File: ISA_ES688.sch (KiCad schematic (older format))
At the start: 112 parts, among them J1 LINE IN, J11 ISA BUS, J2 LINE OUT, J3 Joystick/MIDI, J7 SPKR OUT, J8 MIC, U1 L78L05, U2 74LS14, U7 LM1877, Y1 14.318Mhz

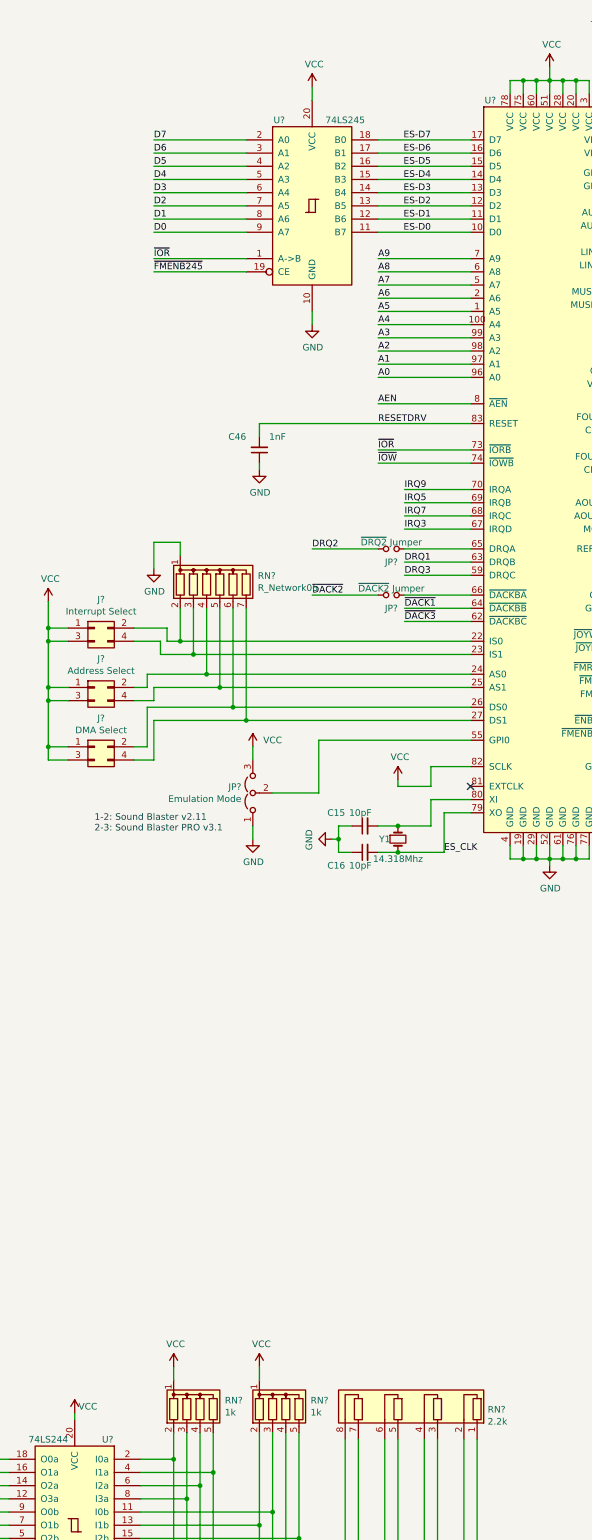
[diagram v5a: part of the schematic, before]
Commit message: Begin assigning footprints
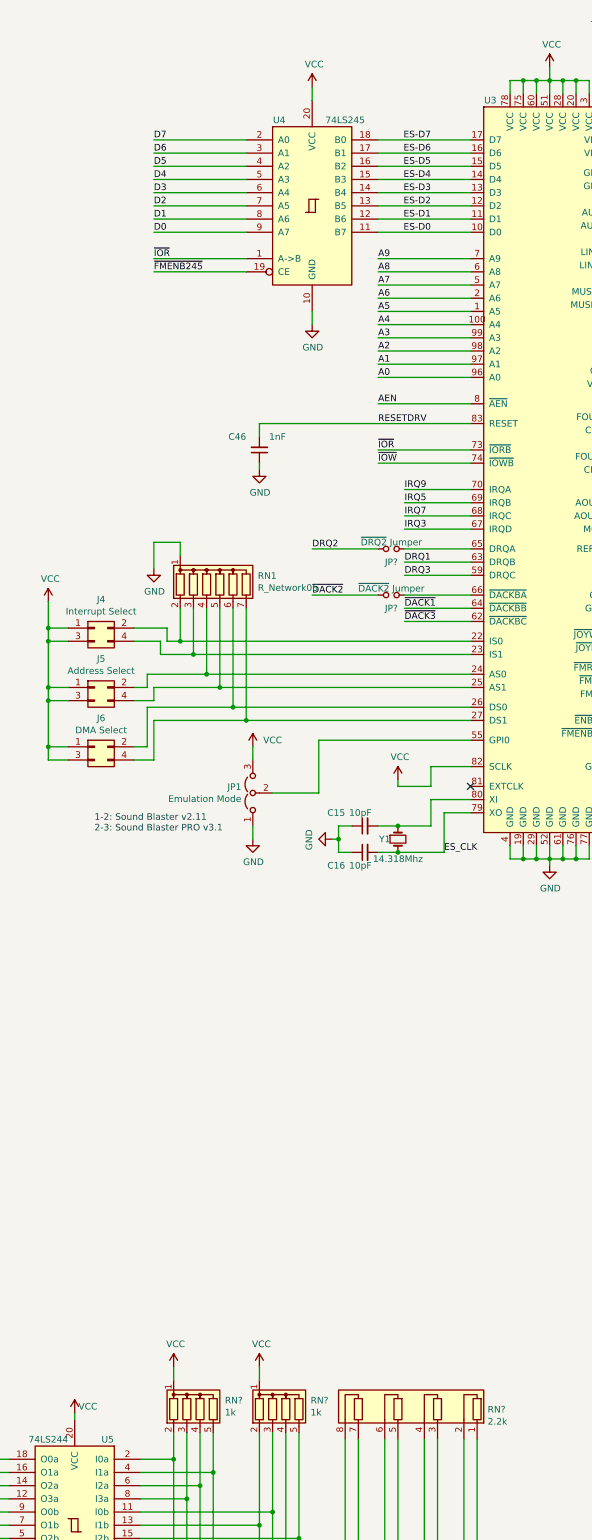
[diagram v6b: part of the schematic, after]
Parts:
- J4, J5, J6: renamed from J?; footprint (none) -> Connector_PinHeader_2.54mm:PinHeader_2x02_P2.54mm_Vertical
- JP1: renamed from JP?; footprint (none) -> Connector_PinHeader_2.54mm:PinHeader_1x03_P2.54mm_Vertical
- RV1: footprint (none) -> Volume_Pot:PTD902
- U4, U5: renamed from U?; footprint (none) -> Package_SO:SOIC-20W_7.5x12.8mm_P1.27mm
- gave numbers to parts that had none: 2
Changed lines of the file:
@@
 NoConn ~ 2300 8550
 $Comp
-L 74xx:74LS245 U?
+L 74xx:74LS245 U4
 U 1 1 60CF4739
 P 10200 2300
-F 0 "U?" H 9950 2950 50  0000 C CNN
+F 0 "U4" H 9950 2950 50  0000 C CNN
 F 1 "74LS245" H 10450 2950 50  0000 C CNN
-F 2 "" H 10200 2300 50  0001 C CNN
+F 2 "Package_SO:SOIC-20W_7.5x12.8mm_P1.27mm" H 10200 2300 50  0001 C CNN
 F 3 "http://www.ti.com/lit/gpn/sn74LS245" H 10200 2300 50  0001 C CNN
 	1    10200 2300
@@
 $EndComp
 $Comp
-L 74xx:74LS244 U?
+L 74xx:74LS244 U5
 U 1 1 60CF5E2D
 P 8400 12300
-F 0 "U?" H 8150 12950 50  0000 C CNN
+F 0 "U5" H 8150 12950 50  0000 C CNN
 F 1 "74LS244" H 8600 12950 50  0000 C CNN
-F 2 "" H 8400 12300 50  0001 C CNN
+F 2 "Package_SO:SOIC-20W_7.5x12.8mm_P1.27mm" H 8400 12300 50  0001 C CNN
 F 3 "http://www.ti.com/lit/ds/symlink/sn74ls244.pdf" H 8400 12300 50  0001 C CNN
 	1    8400 12300
@@
 $EndComp
 $Comp
-L custom_components:ES688F U?
+L custom_components:ES688F U3
 U 1 1 60CF110B
 P 12000 4400
-F 0 "U?" H 11550 7300 50  0000 C CNN
+F 0 "U3" H 11550 7300 50  0000 C CNN
 F 1 "ES688F" H 12500 7300 50  0000 C CNN
 F 2 "Package_QFP:LQFP-14x20mm_P0.5mm" H 12000 5350 50  0001 C CNN
@@
 	11400 5350 10900 5350
 $Comp
-L Connector_Generic:Conn_02x02_Odd_Even J?
+L Connector_Generic:Conn_02x02_Odd_Even J4
 U 1 1 62AED216
 P 8550 5500
-F 0 "J?" H 8600 5717 50  0000 C CNN
+F 0 "J4" H 8600 5717 50  0000 C CNN
 F 1 "Interrupt Select" H 8600 5626 50  0000 C CNN
-F 2 "" H 8550 5500 50  0001 C CNN
+F 2 "Connector_PinHeader_2.54mm:PinHeader_2x02_P2.54mm_Vertical" H 8550 5500 50  0001 C CNN
 F 3 "~" H 8550 5500 50  0001 C CNN
 	1    8550 5500
@@
 	9000 4850 9000 5050
 $Comp
-L Connector_Generic:Conn_02x02_Odd_Even J?
+L Connector_Generic:Conn_02x02_Odd_Even J5
 U 1 1 62BE0014
 P 8550 5950
-F 0 "J?" H 8600 6167 50  0000 C CNN
+F 0 "J5" H 8600 6167 50  0000 C CNN
 F 1 "Address Select" H 8600 6076 50  0000 C CNN
-F 2 "" H 8550 5950 50  0001 C CNN
+F 2 "Connector_PinHeader_2.54mm:PinHeader_2x02_P2.54mm_Vertical" H 8550 5950 50  0001 C CNN
 F 3 "~" H 8550 5950 50  0001 C CNN
 	1    8550 5950
@@
 $EndComp
 $Comp
-L Connector_Generic:Conn_02x02_Odd_Even J?
+L Connector_Generic:Conn_02x02_Odd_Even J6
 U 1 1 62BE0F99
 P 8550 6400
-F 0 "J?" H 8600 6617 50  0000 C CNN
+F 0 "J6" H 8600 6617 50  0000 C CNN
 F 1 "DMA Select" H 8600 6526 50  0000 C CNN
-F 2 "" H 8550 6400 50  0001 C CNN
+F 2 "Connector_PinHeader_2.54mm:PinHeader_2x02_P2.54mm_Vertical" H 8550 6400 50  0001 C CNN
 F 3 "~" H 8550 6400 50  0001 C CNN
 	1    8550 6400
@@
 Connection ~ 13850 1000
 $Comp
-L Device:R_Network06 RN?
+L Device:R_Network06 RN1
 U 1 1 674F16B7
 P 9500 5150
-F 0 "RN?" H 9788 5196 50  0000 L CNN
+F 0 "RN1" H 9788 5196 50  0000 L CNN
 F 1 "R_Network06" H 9788 5105 50  0000 L CNN
 F 2 "Resistor_THT:R_Array_SIP7" V 9875 5150 50  0001 C CNN
@@
 Connection ~ 20900 10250
 $Comp
-L Jumper:Jumper_3_Open JP?
+L Jumper:Jumper_3_Open JP1
 U 1 1 62275D16
 P 9750 6750
-F 0 "JP?" V 9796 6837 50  0000 L CNN
+F 0 "JP1" V 9796 6837 50  0000 L CNN
 F 1 "Emulation Mode" V 9705 6837 50  0000 L CNN
-F 2 "" H 9750 6750 50  0001 C CNN
+F 2 "Connector_PinHeader_2.54mm:PinHeader_1x03_P2.54mm_Vertical" H 9750 6750 50  0001 C CNN
 F 3 "~" H 9750 6750 50  0001 C CNN
 	1    9750 6750
@@
 F 0 "RV1" V 17950 4450 50  0000 R CNN
 F 1 "Volume Knob" V 17850 4750 50  0000 R CNN
-F 2 "" H 17650 4175 50  0001 C CNN
+F 2 "Volume_Pot:PTD902" H 17650 4175 50  0001 C CNN
 F 3 "~" H 17650 4175 50  0001 C CNN
 	1    17400 4250

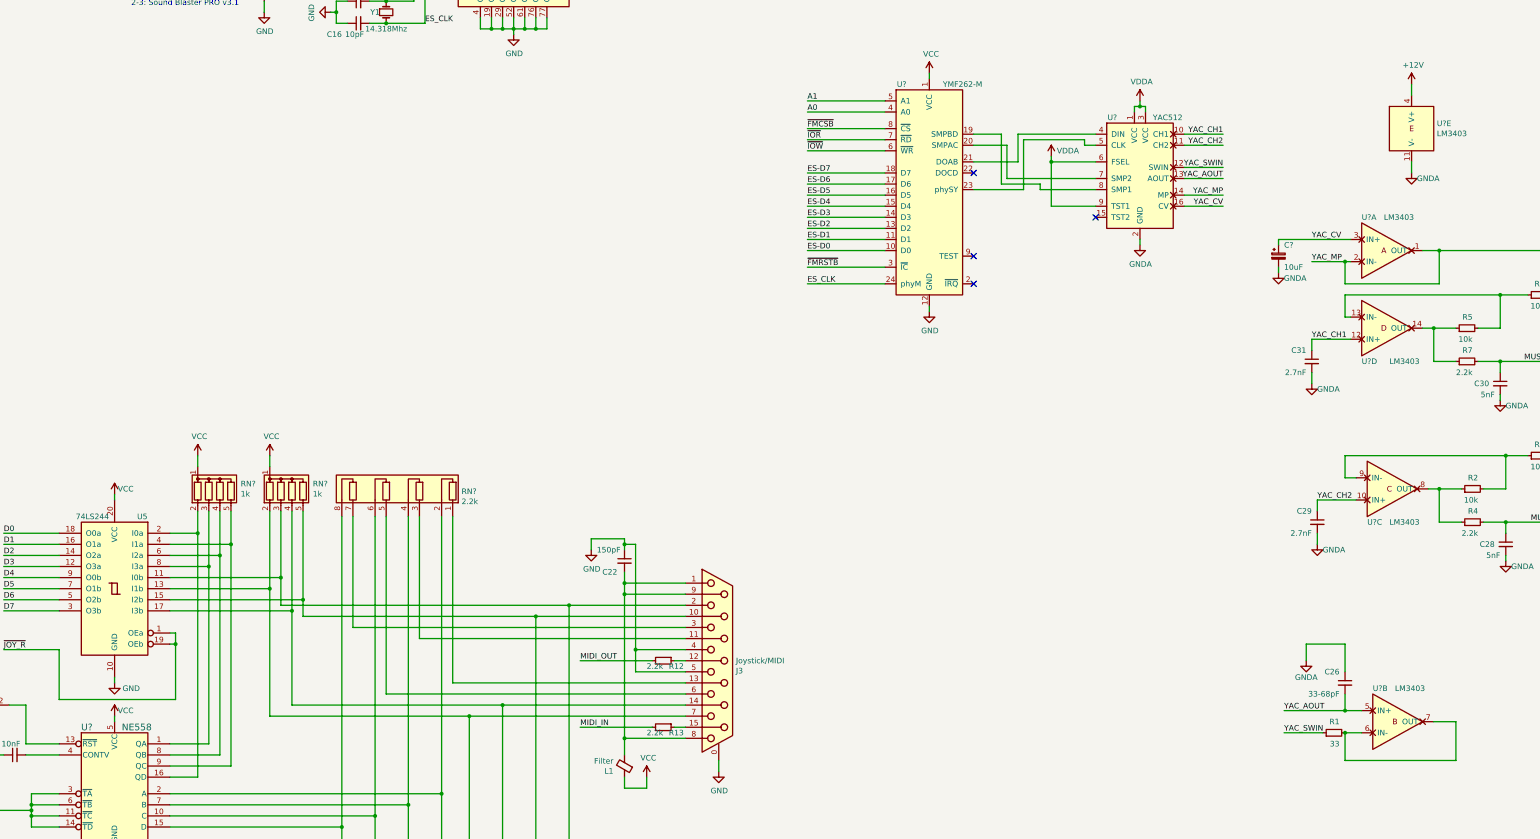
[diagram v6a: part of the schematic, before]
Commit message: Assign more footprints
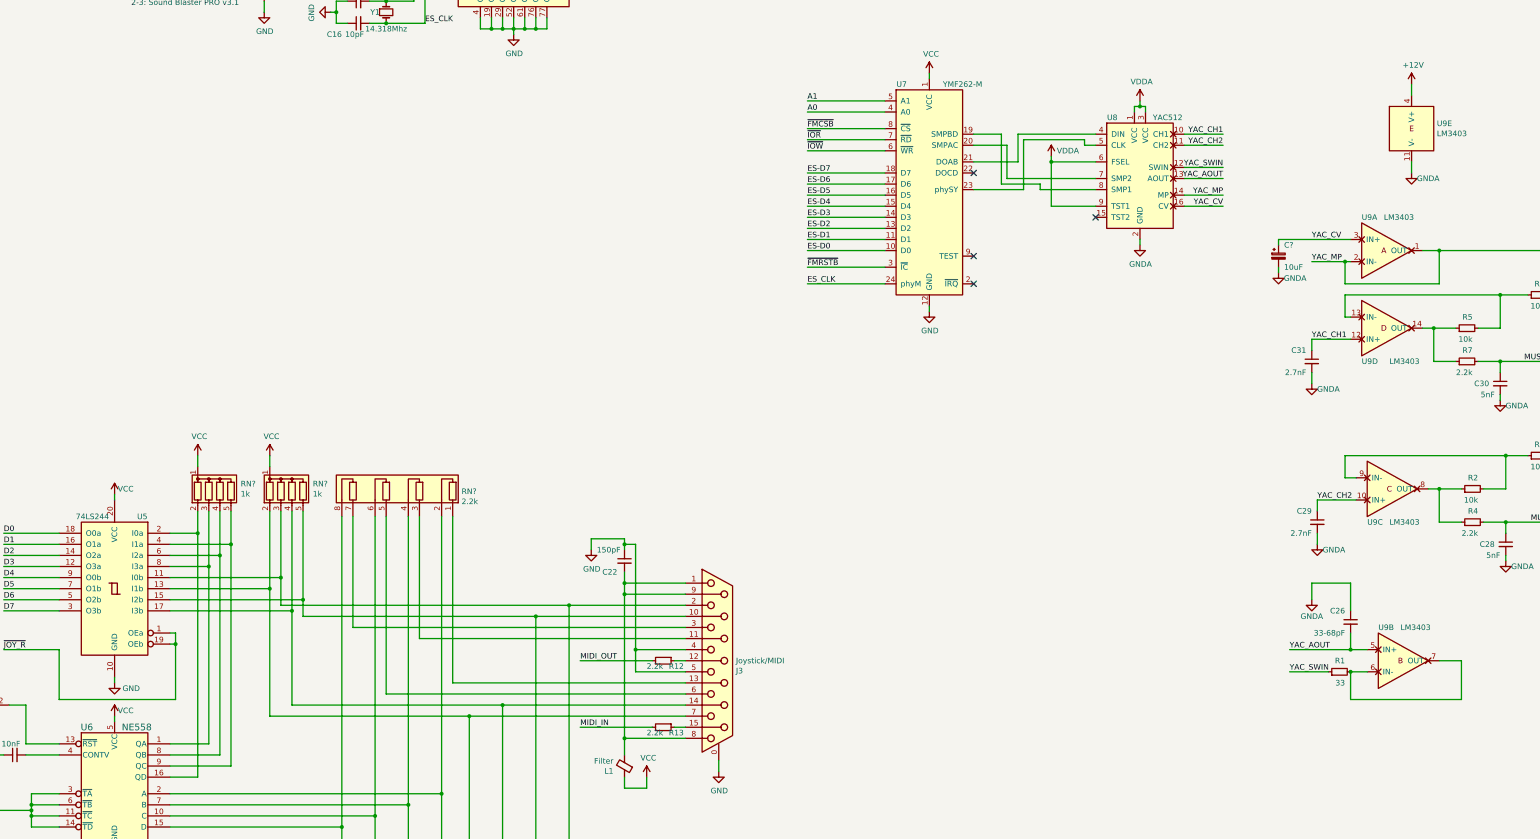
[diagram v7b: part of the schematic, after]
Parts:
- U7: renamed from U?; footprint (none) -> Package_SO:SOIC-24W_7.5x15.4mm_P1.27mm
- U8: renamed from U?; footprint (none) -> Package_SO:SO-16_3.9x9.9mm_P1.27mm
- U9: renamed from U?; footprint (none) -> Package_DIP:DIP-14_W7.62mm
- gave numbers to parts that had none: 1
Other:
- moved on the sheet: C26, R1, U9B
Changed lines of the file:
@@
 $EndComp
 $Comp
-L custom_components:NE558 U?
+L custom_components:NE558 U6
 U 1 1 60D93AFC
 P 8400 14300
-F 0 "U?" H 8150 15050 60  0000 C CNN
+F 0 "U6" H 8150 15050 60  0000 C CNN
 F 1 "NE558" H 8600 15050 60  0000 C CNN
 F 2 "" H 8900 14500 60  0000 C CNN
@@
 $EndComp
 $Comp
-L custom_components:YMF262-M U?
+L custom_components:YMF262-M U7
 U 1 1 675C24EF
 P 15750 8650
-F 0 "U?" H 15500 9550 50  0000 C CNN
+F 0 "U7" H 15500 9550 50  0000 C CNN
 F 1 "YMF262-M" H 16050 9550 50  0000 C CNN
-F 2 "" H 15750 8650 50  0001 C CNN
+F 2 "Package_SO:SOIC-24W_7.5x15.4mm_P1.27mm" H 15750 8650 50  0001 C CNN
 F 3 "" H 15750 8650 50  0001 C CNN
 	1    15750 8650
@@
 $EndComp
 $Comp
-L custom_components:YAC512 U?
+L custom_components:YAC512 U8
 U 1 1 675C3A96
 P 17650 8550
-F 0 "U?" H 17400 9050 50  0000 C CNN
+F 0 "U8" H 17400 9050 50  0000 C CNN
 F 1 "YAC512" H 17900 9050 50  0000 C CNN
-F 2 "" H 17650 7950 50  0001 C CNN
+F 2 "Package_SO:SO-16_3.9x9.9mm_P1.27mm" H 17650 7950 50  0001 C CNN
 F 3 "" H 17650 7950 50  0001 C CNN
 	1    17650 8550
@@
 $EndComp
 $Comp
-L custom_components:LM3403 U?
+L custom_components:LM3403 U9
 U 5 1 675C4E4C
 P 20100 8150
-F 0 "U?" H 20328 8196 50  0000 L CNN
+F 0 "U9" H 20328 8196 50  0000 L CNN
 F 1 "LM3403" H 20328 8105 50  0000 L CNN
-F 2 "" H 20100 8150 50  0001 C CNN
+F 2 "Package_DIP:DIP-14_W7.62mm" H 20100 8150 50  0001 C CNN
 F 3 "" H 20100 8150 50  0001 C CNN
 	5    20100 8150
@@
 NoConn ~ 16150 8550
 $Comp
-L custom_components:LM3403 U?
+L custom_components:LM3403 U9
 U 1 1 618A860C
 P 19850 9250
-F 0 "U?" H 19650 9550 50  0000 L CNN
+F 0 "U9" H 19650 9550 50  0000 L CNN
 F 1 "LM3403" H 19850 9550 50  0000 L CNN
-F 2 "" H 19850 9250 50  0001 C CNN
+F 2 "Package_DIP:DIP-14_W7.62mm" H 19850 9250 50  0001 C CNN
 F 3 "" H 19850 9250 50  0001 C CNN
 	1    19850 9250
@@
 $EndComp
 $Comp
-L custom_components:LM3403 U?
+L custom_components:LM3403 U9
 U 2 1 618ABB59
-P 19950 13500
-F 0 "U?" H 19750 13800 50  0000 L CNN
-F 1 "LM3403" H 19950 13800 50  0000 L CNN
-F 2 "" H 19950 13500 50  0001 C CNN
-F 3 "" H 19950 13500 50  0001 C CNN
-	2    19950 13500
-	1    0    0    -1
-$EndComp
-$Comp
-L custom_components:LM3403 U?
+P 20000 12950
+F 0 "U9" H 19800 13250 50  0000 L CNN
+F 1 "LM3403" H 20000 13250 50  0000 L CNN
+F 2 "Package_DIP:DIP-14_W7.62mm" H 20000 12950 50  0001 C CNN
+F 3 "" H 20000 12950 50  0001 C CNN
+	2    20000 12950
+	1    0    0    -1
+$EndComp
+$Comp
+L custom_components:LM3403 U9
 U 3 1 6191F91E
 P 19900 11400
-F 0 "U?" H 19700 11700 50  0000 L CNN
+F 0 "U9" H 19700 11700 50  0000 L CNN
 F 1 "LM3403" H 19900 11700 50  0000 L CNN
-F 2 "" H 19900 11400 50  0001 C CNN
+F 2 "Package_DIP:DIP-14_W7.62mm" H 19900 11400 50  0001 C CNN
 F 3 "" H 19900 11400 50  0001 C CNN
 	3    19900 11400
@@
 YAC_CH1
 $Comp
-L custom_components:LM3403 U?
+L custom_components:LM3403 U9
 U 4 1 61994965
 P 19850 9950
-F 0 "U?" H 19650 10250 50  0000 L CNN
+F 0 "U9" H 19650 10250 50  0000 L CNN
 F 1 "LM3403" H 19900 10250 50  0000 L CNN
-F 2 "" H 19850 9950 50  0001 C CNN
+F 2 "Package_DIP:DIP-14_W7.62mm" H 19850 9950 50  0001 C CNN
 F 3 "" H 19850 9950 50  0001 C CNN
 	4    19850 9950
@@
 Text Label 18400 8600 2    50   ~ 0
 YAC_AOUT
-Text Label 18950 13400 0    50   ~ 0
+Text Label 19000 12850 0    50   ~ 0
 YAC_AOUT
 Wire Wire Line
-	18950 13400 19500 13400
+	19000 12850 19550 12850
 $Comp
 L Device:C_Small C26
 U 1 1 62A2E09E
-P 19500 13150
-F 0 "C26" H 19550 13250 50  0000 L CNN
-F 1 "33-68pF" H 19550 13050 50  0000 L CNN
-F 2 "Capacitor_THT:C_Disc_D6.0mm_W2.5mm_P5.00mm" H 19500 13150 50  0001 C CNN
-F 3 "~" H 19500 13150 50  0001 C CNN
-	1    19500 13150
+P 19550 12600
+F 0 "C26" H 19600 12700 50  0000 L CNN
+F 1 "33-68pF" H 19600 12500 50  0000 L CNN
+F 2 "Capacitor_THT:C_Disc_D6.0mm_W2.5mm_P5.00mm" H 19550 12600 50  0001 C CNN
+F 3 "~" H 19550 12600 50  0001 C CNN
+	1    19550 12600
 	-1   0    0    -1
 $EndComp
 Wire Wire Line
-	19500 13250 19500 13400
-Connection ~ 19500 13400
-Wire Wire Line
-	19500 13400 19650 13400
+	19550 12700 19550 12850
+Connection ~ 19550 12850
+Wire Wire Line
+	19550 12850 19700 12850
 $Comp
 L power:GNDA #PWR?
 U 1 1 62AAAABD
-P 19150 12950
-F 0 "#PWR?" H 19150 12700 50  0001 C CNN
-F 1 "GNDA" H 19150 12800 50  0000 C CNN
-F 2 "" H 19150 12950 50  0001 C CNN
-F 3 "" H 19150 12950 50  0001 C CNN
-	1    19150 12950
-	1    0    0    -1
-$EndComp
-Wire Wire Line
-	19500 13050 19500 12800
-Wire Wire Line
-	19500 12800 19150 12800
-Wire Wire Line
-	19150 12800 19150 12950
-Wire Wire Line
-	20300 13500 20500 13500
-Wire Wire Line
-	20500 13500 20500 13850
-Wire Wire Line
-	20500 13850 19500 13850
-Wire Wire Line
-	19500 13850 19500 13600
-Wire Wire Line
-	19500 13600 19650 13600
+P 19200 12400
+F 0 "#PWR?" H 19200 12150 50  0001 C CNN
+F 1 "GNDA" H 19200 12250 50  0000 C CNN
+F 2 "" H 19200 12400 50  0001 C CNN
+F 3 "" H 19200 12400 50  0001 C CNN
+	1    19200 12400
+	1    0    0    -1
+$EndComp
+Wire Wire Line
+	19550 12500 19550 12250
+Wire Wire Line
+	19550 12250 19200 12250
+Wire Wire Line
+	19200 12250 19200 12400
+Wire Wire Line
+	20350 12950 20550 12950
+Wire Wire Line
+	20550 12950 20550 13300
+Wire Wire Line
+	20550 13300 19550 13300
+Wire Wire Line
+	19550 13300 19550 13050
+Wire Wire Line
+	19550 13050 19700 13050
 $Comp
 L Device:R_Small R1
 U 1 1 62CA2E14
-P 19400 13600
-F 0 "R1" V 19500 13550 50  0000 L CNN
-F 1 "33" V 19300 13550 50  0000 L CNN
-F 2 "Resistor_THT:R_Axial_DIN0207_L6.3mm_D2.5mm_P7.62mm_Horizontal" H 19400 13600 50  0001 C CNN
-F 3 "~" H 19400 13600 50  0001 C CNN
-	1    19400 13600
+P 19450 13050
+F 0 "R1" V 19550 13000 50  0000 L CNN
+F 1 "33" V 19350 13000 50  0000 L CNN
+F 2 "Resistor_THT:R_Axial_DIN0207_L6.3mm_D2.5mm_P7.62mm_Horizontal" H 19450 13050 50  0001 C CNN
+F 3 "~" H 19450 13050 50  0001 C CNN
+	1    19450 13050
 	0    -1   -1   0
 $EndComp
-Connection ~ 19500 13600
-Wire Wire Line
-	19300 13600 18950 13600
-Text Label 18950 13600 0    50   ~ 0
+Connection ~ 19550 13050
+Wire Wire Line
+	19350 13050 19000 13050
+Text Label 19000 13050 0    50   ~ 0
 YAC_SWIN
 Wire Wire Line
